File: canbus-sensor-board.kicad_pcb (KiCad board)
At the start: 4 copper layers, 32 x 39 mm, 51 parts, among them J1 CAN IO, J10 Conn_01x01, J11 Conn_01x01, J2 CAN Term, J3 POWER IN, J4 Conn_01x01, J5 I2C2 IO, J6 I2C1 IO, J7 Conn_01x01, J8 Conn_ARM_SWD_TagConnect_TC203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, J9 Conn_01x01, Q1 2N7002, Q2 2N7002, Q3 2N7002, Q4 2N7002, U1 MCP2551-I-SN, U3 AMS1117-3.3, U4 STM32F103C8Tx

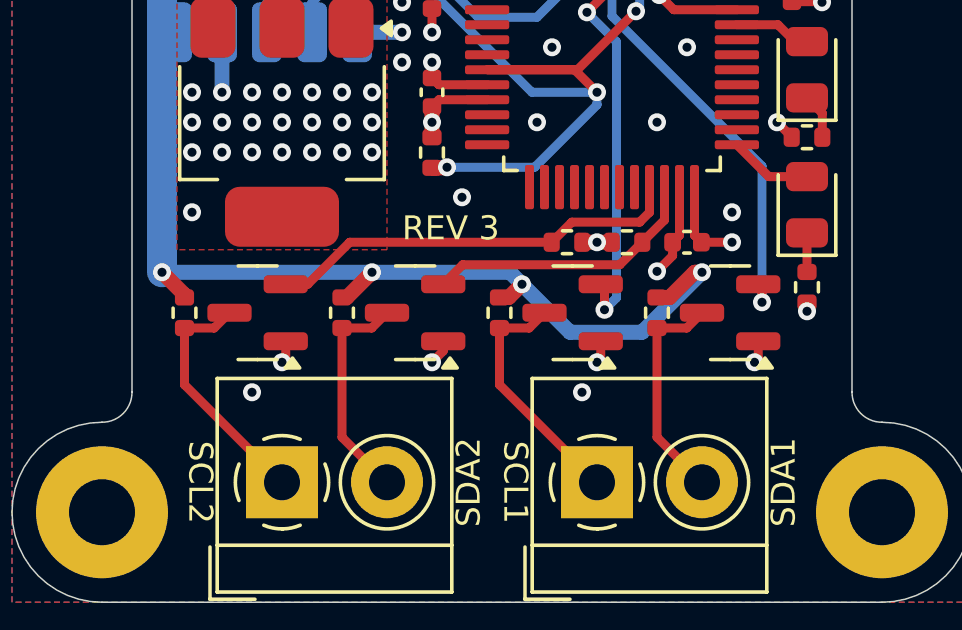
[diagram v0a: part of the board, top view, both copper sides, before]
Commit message: Switch to MOSFETs with lower Vgs thresholds
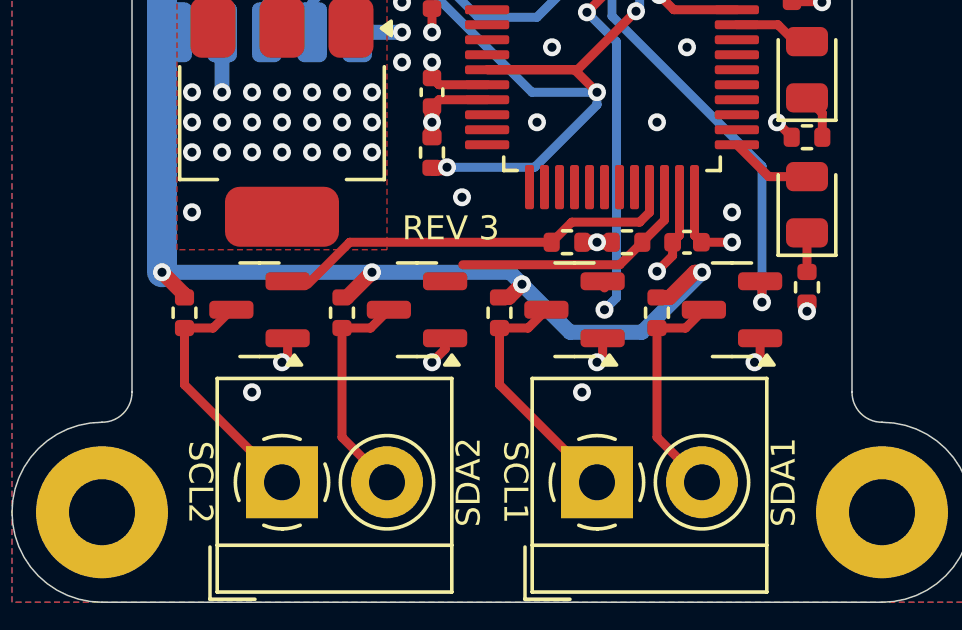
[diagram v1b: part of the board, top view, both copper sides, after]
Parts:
- Q1, Q2, Q3, Q4: value 2N7002 -> AO3400A
- moved Q1 0.12 mm to (38.8, 59.2)
- moved Q2 0.12 mm to (44.0, 59.2)
- moved Q3 0.12 mm to (28.2, 59.2)
- moved Q4 0.12 mm to (33.5, 59.2)
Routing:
- net I2C2_SDA: track 9.36 -> 8.44 mm
- net I2C2_SCL: track 14.0 -> 13.2 mm
- net I2C1_SCL: track 16.5 -> 15.8 mm
- net +3.3V: track 34.7 -> 35.2 mm

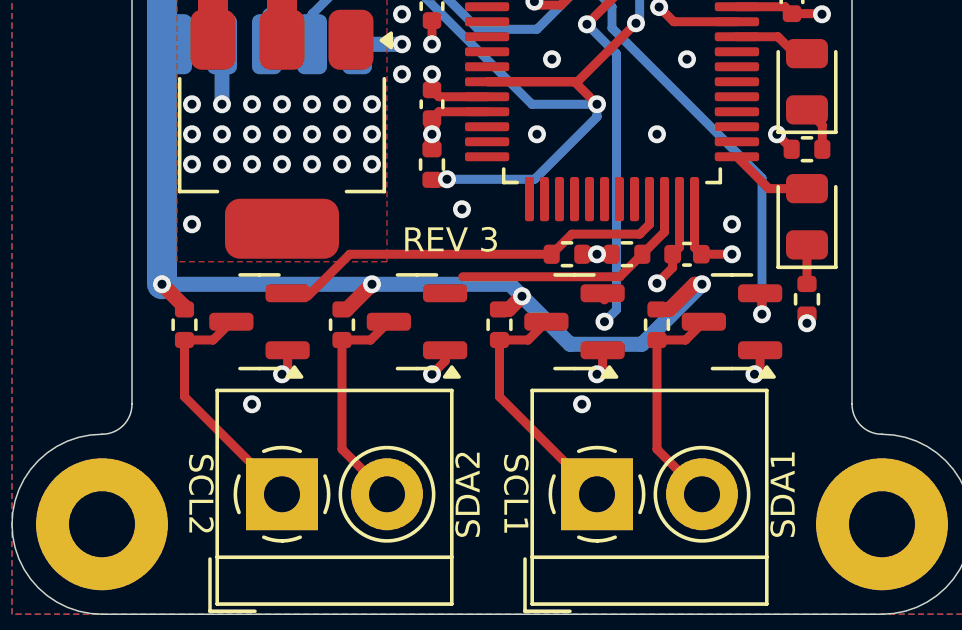
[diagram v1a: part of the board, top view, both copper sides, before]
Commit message: Fix some broken tracks
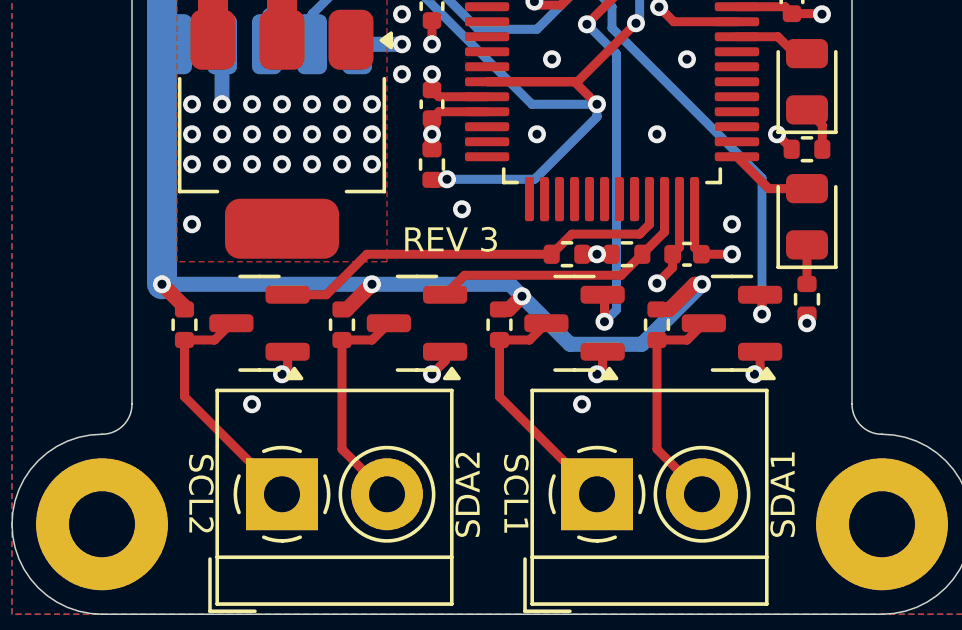
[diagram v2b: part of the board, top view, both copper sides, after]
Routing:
- net I2C2_SDA: track 8.44 -> 9.28 mm
- net I2C1_SCL: track 15.8 -> 16.5 mm
- net I2C2_SCL: track 13.2 -> 13.9 mm
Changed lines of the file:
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@@
 	(footprint "Package_TO_SOT_SMD:SOT-23"
 		(layer "F.Cu")
-		(at 33.5 59.25 180)
+		(at 33.5 59.3 180)
 		(descr "SOT, 3 Pin (https://www.jedec.org/system/files/docs/to-236h.pdf variant AB), generated with kicad-footprint-generator ipc_gullwing_generator.py")
 		(tags "SOT TO_SOT_SMD")
@@
 	(footprint "Package_TO_SOT_SMD:SOT-23"
 		(layer "F.Cu")
-		(at 38.75 59.25 180)
+		(at 38.75 59.3 180)
 		(descr "SOT, 3 Pin (https://www.jedec.org/system/files/docs/to-236h.pdf variant AB), generated with kicad-footprint-generator ipc_gullwing_generator.py")
 		(tags "SOT TO_SOT_SMD")
@@
 	(footprint "Package_TO_SOT_SMD:SOT-23"
 		(layer "F.Cu")
-		(at 28.25 59.25 180)
+		(at 28.25 59.3 180)
 		(descr "SOT, 3 Pin (https://www.jedec.org/system/files/docs/to-236h.pdf variant AB), generated with kicad-footprint-generator ipc_gullwing_generator.py")
 		(tags "SOT TO_SOT_SMD")
@@
 	(footprint "Package_TO_SOT_SMD:SOT-23"
 		(layer "F.Cu")
-		(at 44 59.25 180)
+		(at 44 59.3 180)
 		(descr "SOT, 3 Pin (https://www.jedec.org/system/files/docs/to-236h.pdf variant AB), generated with kicad-footprint-generator ipc_gullwing_generator.py")
 		(tags "SOT TO_SOT_SMD")
@@
 	)
 	(segment
-		(start 44.9375 60.2)
-		(end 44.9375 60.8125)
-		(width 0.3)
-		(layer "F.Cu")
-		(net 10)
-	)
-	(segment
 		(start 35 47.5)
 		(end 35 47.4)
@@
 	)
 	(segment
-		(start 31.4625 47.4375)
-		(end 31.5 47.475)
-		(width 1)
+		(start 29.1875 60.25)
+		(end 29.1875 60.8125)
+		(width 0.3)
 		(layer "F.Cu")
 		(net 10)
 	)
 	(segment
-		(start 35.8375 52.25)
-		(end 34.23 52.25)
+		(start 29.1875 60.8125)
+		(end 29 61)
 		(width 0.3)
 		(layer "F.Cu")
@@
 	)
 	(segment
-		(start 35.8375 48.25)
-		(end 35.75 48.25)
+		(start 31.4625 47.4375)
+		(end 31.5 47.475)
+		(width 1)
+		(layer "F.Cu")
+		(net 10)
+	)
+	(segment
+		(start 44.9375 60.8125)
+		(end 44.75 61)
 		(width 0.3)
 		(layer "F.Cu")
@@
 	)
 	(segment
-		(start 29.1875 60.2)
-		(end 29.1875 60.8125)
+		(start 35.8375 52.25)
+		(end 34.23 52.25)
 		(width 0.3)
 		(layer "F.Cu")
@@
 	)
 	(segment
-		(start 34.4375 60.5625)
-		(end 34 61)
+		(start 35.8375 48.25)
+		(end 35.75 48.25)
 		(width 0.3)
 		(layer "F.Cu")
@@
 	)
 	(segment
-		(start 39.6875 60.8125)
-		(end 39.5 61)
+		(start 34.4375 60.5625)
+		(end 34 61)
 		(width 0.3)
 		(layer "F.Cu")
@@
 	)
 	(segment
-		(start 34.4375 60.2)
-		(end 34.4375 60.5625)
-		(width 0.3)
-		(layer "F.Cu")
-		(net 10)
-	)
-	(segment
 		(start 29 49.85)
 		(end 29 47.4375)
@@
 	)
 	(segment
+		(start 39.6875 60.8125)
+		(end 39.5 61)
+		(width 0.3)
+		(layer "F.Cu")
+		(net 10)
+	)
+	(segment
 		(start 37.02 45)
 		(end 36.5 45)
@@
 	)
 	(segment
-		(start 44.9375 60.8125)
-		(end 44.75 61)
+		(start 34.4375 60.25)
+		(end 34.4375 60.5625)
 		(width 0.3)
 		(layer "F.Cu")
@@
 	)
 	(segment
-		(start 29.1875 60.8125)
-		(end 29 61)
-		(width 0.3)
-		(layer "F.Cu")
-		(net 10)
-	)
-	(segment
 		(start 35.75 48.25)
 		(end 35 47.5)
@@
 	)
 	(segment
+		(start 44.9375 60.25)
+		(end 44.9375 60.8125)
+		(width 0.3)
+		(layer "F.Cu")
+		(net 10)
+	)
+	(segment
+		(start 39.6875 60.25)
+		(end 39.6875 60.8125)
+		(width 0.3)
+		(layer "F.Cu")
+		(net 10)
+	)
+	(segment
 		(start 32.125 47.475)
 		(end 33.6 46)
@@
 		(net 10)
 	)
-	(segment
-		(start 39.6875 60.2)
-		(end 39.6875 60.8125)
-		(width 0.3)
-		(layer "F.Cu")
-		(net 10)
-	)
 	(via
 		(at 40 43)
@@
 	)
 	(segment
+		(start 45 59)
+		(end 45 58.4125)
+		(width 0.3)
+		(layer "F.Cu")
+		(net 14)
+	)
+	(segment
 		(start 39.75 46.8375)
 		(end 39.75 45.26)
@@
 	)
 	(segment
-		(start 39.75 47.83076)
-		(end 39.41538 48.16538)
+		(start 45 58.4125)
+		(end 44.9375 58.35)
 		(width 0.3)
 		(layer "F.Cu")
@@
 	)
 	(segment
-		(start 39.75 46.8375)
-		(end 39.75 47.83076)
+		(start 39.75 47.83076)
+		(end 39.41538 48.16538)
 		(width 0.3)
 		(layer "F.Cu")
@@
 	)
 	(segment
-		(start 45 59)
-		(end 45 58.525)
+		(start 39.75 46.8375)
+		(end 39.75 47.83076)
 		(width 0.3)
 		(layer "F.Cu")
@@
 	)
 	(segment
-		(start 40.26 57.75)
-		(end 35.025 57.75)
+		(start 40.31 57.7)
+		(end 35.0875 57.7)
 		(width 0.3)
 		(layer "F.Cu")
@@
 	)
 	(segment
+		(start 35.0875 57.7)
+		(end 34.4375 58.35)
+		(width 0.3)
+		(layer "F.Cu")
+		(net 20)
+	)
+	(segment
 		(start 41.75 56.26)
 		(end 41.01 57)
@@
 	(segment
 		(start 41.01 57)
-		(end 40.26 57.75)
+		(end 40.31 57.7)
 		(width 0.3)
 		(layer "F.Cu")
@@
 	)
 	(segment
-		(start 39.75 58.525)
-		(end 39.625 58.4)
+		(start 40.25 46.8375)
+		(end 40.25 48.25)
 		(width 0.3)
 		(layer "F.Cu")
@@
 	)
 	(segment
-		(start 40.25 46.8375)
-		(end 40.25 48.25)
+		(start 39.75 59.25)
+		(end 39.75 58.4125)
 		(width 0.3)
 		(layer "F.Cu")
@@
 		(net 22)
 	)
+	(segment
+		(start 39.75 58.4125)
+		(end 39.6875 58.35)
+		(width 0.3)
+		(layer "F.Cu")
+		(net 22)
+	)
 	(via
 		(at 39.75 59.25)
@@
 	)
 	(segment
-		(start 41.25 55.1625)
-		(end 41.25 56.00312)
+		(start 30.480366 58.35)
+		(end 29.1875 58.35)
 		(width 0.3)
 		(layer "F.Cu")
@@
 	)
 	(segment
-		(start 40.92312 56.33)
-		(end 38.66 56.33)
+		(start 37.99 57)
+		(end 31.830366 57)
 		(width 0.3)
 		(layer "F.Cu")
@@
 	)
 	(segment
-		(start 31.259354 57)
-		(end 29.859354 58.4)
+		(start 41.25 55.1625)
+		(end 41.25 56.00312)
 		(width 0.3)
 		(layer "F.Cu")
@@
 	)
 	(segment
-		(start 37.99 57)
-		(end 31.259354 57)
+		(start 40.92312 56.33)
+		(end 38.66 56.33)
+		(width 0.3)
+		(layer "F.Cu")
+		(net 34)
+	)
+	(segment
+		(start 31.830366 57)
+		(end 30.480366 58.35)
 		(width 0.3)
 		(layer "F.Cu")
@@
 	)
 	(segment
-		(start 25.75 61.75)
-		(end 29 65)
+		(start 26.7525 59.86)
+		(end 27.3125 59.3)
 		(width 0.3)
 		(layer "F.Cu")
@@
 	)
 	(segment
-		(start 25.75 59.86)
-		(end 26.7025 59.86)
+		(start 25.75 61.75)
+		(end 29 65)
 		(width 0.3)
 		(layer "F.Cu")
@@
 	)
 	(segment
-		(start 26.7025 59.86)
-		(end 27.3125 59.25)
+		(start 25.75 59.86)
+		(end 26.7525 59.86)
 		(width 0.3)
 		(layer "F.Cu")
@@
 	)
 	(segment
-		(start 31.9525 59.86)
-		(end 32.5625 59.25)
+		(start 32.0025 59.86)
+		(end 32.5625 59.3)
 		(width 0.3)
 		(layer "F.Cu")
@@
 	(segment
 		(start 31 59.86)
-		(end 31.9525 59.86)
+		(end 32.0025 59.86)
 		(width 0.3)
 		(layer "F.Cu")
@@
 	)
 	(segment
-		(start 41.5 63.5)
-		(end 43 65)
+		(start 41.5 59.86)
+		(end 42.5025 59.86)
 		(width 0.3)
 		(layer "F.Cu")
@@
 	)
 	(segment
-		(start 41.5 59.86)
-		(end 42.4525 59.86)
+		(start 41.5 63.5)
+		(end 43 65)
 		(width 0.3)
 		(layer "F.Cu")
@@
 	)
 	(segment
-		(start 42.4525 59.86)
-		(end 43.0625 59.25)
+		(start 42.5025 59.86)
+		(end 43.0625 59.3)
 		(width 0.3)
 		(layer "F.Cu")
@@
 	)
 	(segment
-		(start 37.2025 59.86)
-		(end 37.8125 59.25)
+		(start 36.25 59.86)
+		(end 36.25 61.75)
 		(width 0.3)
 		(layer "F.Cu")
@@
 	)
 	(segment
-		(start 36.25 59.86)
-		(end 36.25 61.75)
+		(start 37.2525 59.86)
+		(end 37.8125 59.3)
 		(width 0.3)
 		(layer "F.Cu")
@@
 	)
 	(segment
-		(start 36.25 59.86)
-		(end 37.2025 59.86)
+		(start 36.25 61.75)
+		(end 39.5 65)
 		(width 0.3)
 		(layer "F.Cu")
@@
 	)
 	(segment
-		(start 36.25 61.75)
-		(end 39.5 65)
+		(start 36.25 59.86)
+		(end 37.2525 59.86)
 		(width 0.3)
 		(layer "F.Cu")
